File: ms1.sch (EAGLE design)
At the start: 145 parts, among them IC1 MAX3232EUE, IC2 MAX3380EEUP, J1 POWERPOLE_POWER25A, J10 Radio, J11 A3, J12 A4, J13 A5, J14 A6, J15 A7, J16 D1, J17 D2, J18 D3, J19 D4, J2 ON, J20 D5, J21 D6, J22 D7, J3 LED-EN, J4 RS232, J5 RS485, J6 A1, J7 I2C, J8 A2, J9 TTL_SERIAL, Q1 DMG6602SVT, Q2 DMG6602SVT, Q3 DMG6602SVT, Q4 DMG6602SVT, U1 LT1934ES6TRMPBF, U2 LT1934ES6TRMPBF, U3 DS3231SN, U4 ISL3179EIBZ, X1 KUSBVX-BS1N

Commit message: power supplies mostly routed
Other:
- moved on the sheet: U$2

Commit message: serial stuff laid out
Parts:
- added C26: 100nF, resistor:C-EUC0805
- renumbered VCC_3V1 to VCC_3V
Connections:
- net GND: now also C26.2
- net VCC_3V3: now also C26.1
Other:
- moved on the sheet: U$2

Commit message: added pullup to !RESET on CC1120
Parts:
- added R33: 1K, resistor:R-EU_R0805
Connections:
- new net N$17: R33.1, U$3.!RESET
- net RADIO_3V3: now also R33.2

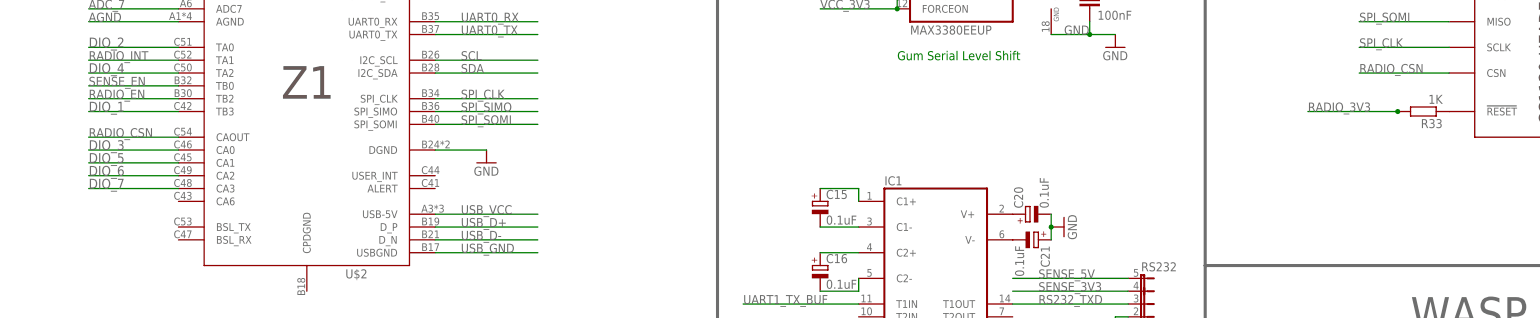
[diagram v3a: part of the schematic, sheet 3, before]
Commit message: added reset link from cc1120 to msp
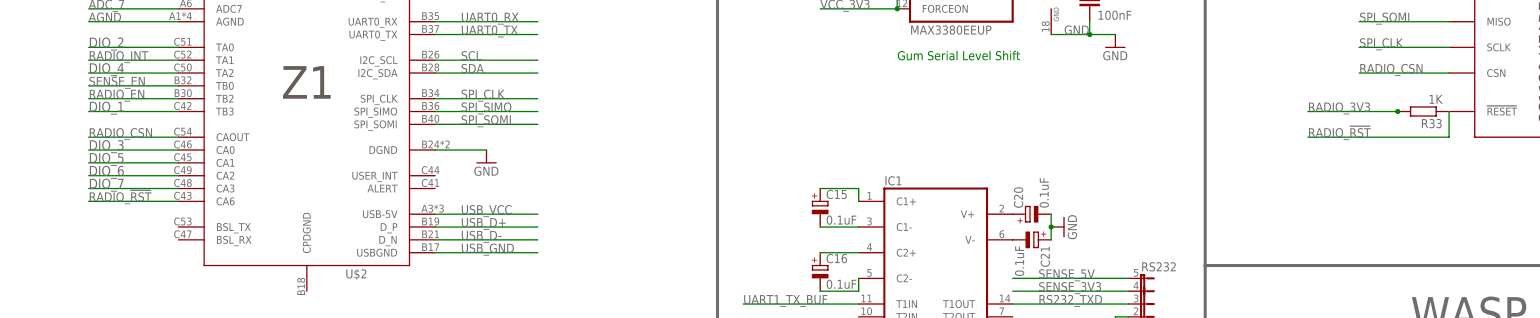
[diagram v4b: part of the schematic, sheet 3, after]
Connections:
- removed net N$17: R33.1, U$3.!RESET
- new net RADIO_!RST: R33.1, U$2.CA6, U$3.!RESET
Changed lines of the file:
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@@
 </segment>
 </net>
-<net name="N$17" class="0">
+<net name="RADIO_!RST" class="0">
+<segment>
+<pinref part="U$2" gate="G$1" pin="CA6"/>
+<wire x1="38.1" y1="167.64" x2="20.32" y2="167.64" width="0.1524" layer="91"/>
+<label x="20.32" y="167.64" size="1.778" layer="95"/>
+</segment>
 <segment>
 <pinref part="U$3" gate="G$1" pin="!RESET"/>
 <pinref part="R33" gate="G$1" pin="1"/>
+<wire x1="289.56" y1="185.42" x2="289.56" y2="180.34" width="0.1524" layer="91"/>
+<wire x1="289.56" y1="180.34" x2="261.62" y2="180.34" width="0.1524" layer="91"/>
+<label x="261.62" y="180.34" size="1.778" layer="95"/>
 </segment>
 </net>

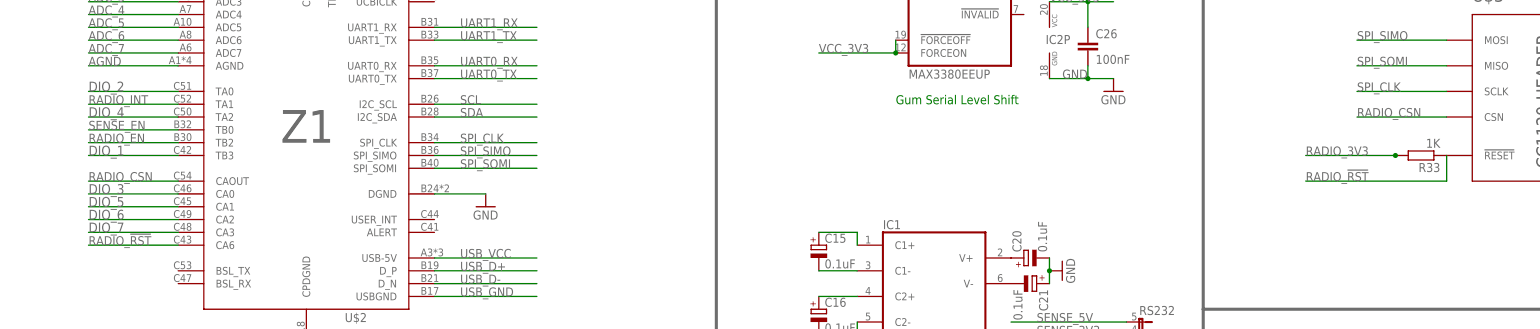
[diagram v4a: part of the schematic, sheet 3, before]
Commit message: cc1120 wiring matches test harness
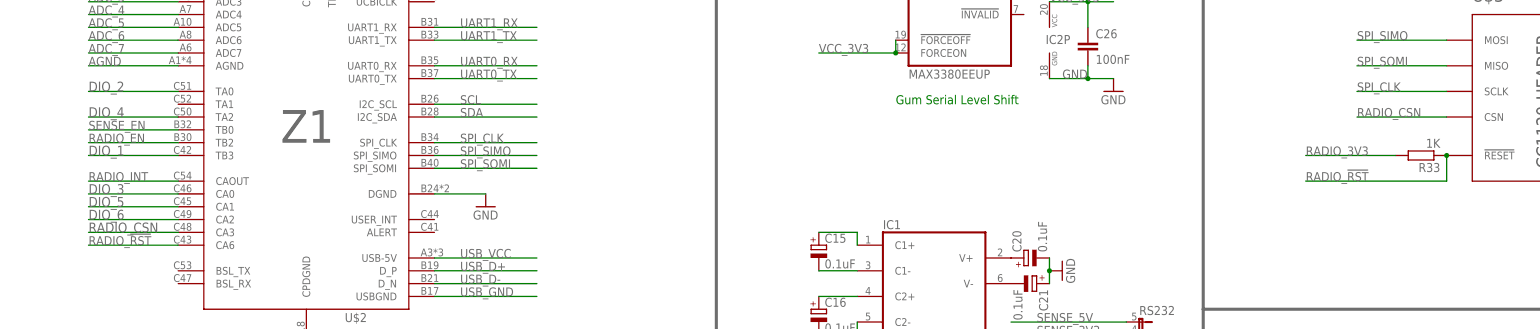
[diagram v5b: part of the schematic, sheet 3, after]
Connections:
- net DIO_7: no longer U$2.CA3
- net RADIO_CSN: now also U$2.CA3; no longer U$2.CAOUT
- net RADIO_INT: now also U$2.CAOUT; no longer U$2.TA1
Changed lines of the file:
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@@
 <label x="261.62" y="185.42" size="1.778" layer="95"/>
 <pinref part="R33" gate="G$1" pin="2"/>
-<junction x="279.4" y="185.42"/>
 </segment>
 </net>
@@
 </segment>
 <segment>
+<pinref part="U$2" gate="G$1" pin="CA3"/>
+<wire x1="38.1" y1="170.18" x2="20.32" y2="170.18" width="0.1524" layer="91"/>
+<label x="20.32" y="170.18" size="1.9304" layer="95"/>
+</segment>
+</net>
+<net name="USB_VCC" class="0">
+<segment>
+<pinref part="U$2" gate="G$1" pin="USB-5V"/>
+<wire x1="88.9" y1="165.1" x2="109.22" y2="165.1" width="0.1524" layer="91"/>
+<label x="93.98" y="165.1" size="1.778" layer="95"/>
+</segment>
+</net>
+<net name="USB_D+" class="0">
+<segment>
+<pinref part="U$2" gate="G$1" pin="D_P"/>
+<wire x1="88.9" y1="162.56" x2="109.22" y2="162.56" width="0.1524" layer="91"/>
+<label x="93.98" y="162.56" size="1.778" layer="95"/>
+</segment>
+</net>
+<net name="USB_D-" class="0">
+<segment>
+<pinref part="U$2" gate="G$1" pin="D_N"/>
+<wire x1="88.9" y1="160.02" x2="109.22" y2="160.02" width="0.1524" layer="91"/>
+<label x="93.98" y="160.02" size="1.778" layer="95"/>
+</segment>
+</net>
+<net name="USB_GND" class="0">
+<segment>
+<pinref part="U$2" gate="G$1" pin="USBGND"/>
+<wire x1="88.9" y1="157.48" x2="109.22" y2="157.48" width="0.1524" layer="91"/>
+<label x="93.98" y="157.48" size="1.778" layer="95"/>
+</segment>
+</net>
+<net name="BATV_EN" class="0">
+<segment>
+<wire x1="203.2" y1="20.32" x2="180.34" y2="20.32" width="0.1524" layer="91"/>
+<label x="182.88" y="20.32" size="1.778" layer="95"/>
+<pinref part="JP1" gate="A" pin="2"/>
+</segment>
+</net>
+<net name="SENSE_EN" class="0">
+<segment>
+<wire x1="203.2" y1="17.78" x2="180.34" y2="17.78" width="0.1524" layer="91"/>
+<label x="182.88" y="17.78" size="1.778" layer="95"/>
+<pinref part="JP1" gate="A" pin="1"/>
+</segment>
+<segment>
+<pinref part="U$2" gate="G$1" pin="TB0"/>
+<wire x1="38.1" y1="190.5" x2="20.32" y2="190.5" width="0.1524" layer="91"/>
+<label x="20.32" y="190.5" size="1.778" layer="95"/>
+</segment>
+</net>
+<net name="RADIO_EN" class="0">
+<segment>
+<wire x1="20.32" y1="187.96" x2="38.1" y2="187.96" width="0.1524" layer="91"/>
+<label x="20.32" y="187.96" size="1.778" layer="95"/>
+<pinref part="U$2" gate="G$1" pin="TB2"/>
+</segment>
+</net>
+<net name="RADIO_INT" class="0">
+<segment>
+<pinref part="U$3" gate="G$1" pin="GPIO0"/>
+<wire x1="327.66" y1="203.2" x2="350.52" y2="203.2" width="0.1524" layer="91"/>
+<label x="342.9" y="203.2" size="1.778" layer="95"/>
+</segment>
+<segment>
 <pinref part="U$2" gate="G$1" pin="CAOUT"/>
 <wire x1="38.1" y1="180.34" x2="20.32" y2="180.34" width="0.1524" layer="91"/>
 <label x="20.32" y="180.34" size="1.778" layer="95"/>
-</segment>
-</net>
-<net name="USB_VCC" class="0">
-<segment>
-<pinref part="U$2" gate="G$1" pin="USB-5V"/>
-<wire x1="88.9" y1="165.1" x2="109.22" y2="165.1" width="0.1524" layer="91"/>
-<label x="93.98" y="165.1" size="1.778" layer="95"/>
-</segment>
-</net>
-<net name="USB_D+" class="0">
-<segment>
-<pinref part="U$2" gate="G$1" pin="D_P"/>
-<wire x1="88.9" y1="162.56" x2="109.22" y2="162.56" width="0.1524" layer="91"/>
-<label x="93.98" y="162.56" size="1.778" layer="95"/>
-</segment>
-</net>
-<net name="USB_D-" class="0">
-<segment>
-<pinref part="U$2" gate="G$1" pin="D_N"/>
-<wire x1="88.9" y1="160.02" x2="109.22" y2="160.02" width="0.1524" layer="91"/>
-<label x="93.98" y="160.02" size="1.778" layer="95"/>
-</segment>
-</net>
-<net name="USB_GND" class="0">
-<segment>
-<pinref part="U$2" gate="G$1" pin="USBGND"/>
-<wire x1="88.9" y1="157.48" x2="109.22" y2="157.48" width="0.1524" layer="91"/>
-<label x="93.98" y="157.48" size="1.778" layer="95"/>
-</segment>
-</net>
-<net name="BATV_EN" class="0">
-<segment>
-<wire x1="203.2" y1="20.32" x2="180.34" y2="20.32" width="0.1524" layer="91"/>
-<label x="182.88" y="20.32" size="1.778" layer="95"/>
-<pinref part="JP1" gate="A" pin="2"/>
-</segment>
-</net>
-<net name="SENSE_EN" class="0">
-<segment>
-<wire x1="203.2" y1="17.78" x2="180.34" y2="17.78" width="0.1524" layer="91"/>
-<label x="182.88" y="17.78" size="1.778" layer="95"/>
-<pinref part="JP1" gate="A" pin="1"/>
-</segment>
-<segment>
-<pinref part="U$2" gate="G$1" pin="TB0"/>
-<wire x1="38.1" y1="190.5" x2="20.32" y2="190.5" width="0.1524" layer="91"/>
-<label x="20.32" y="190.5" size="1.778" layer="95"/>
-</segment>
-</net>
-<net name="RADIO_EN" class="0">
-<segment>
-<wire x1="20.32" y1="187.96" x2="38.1" y2="187.96" width="0.1524" layer="91"/>
-<label x="20.32" y="187.96" size="1.778" layer="95"/>
-<pinref part="U$2" gate="G$1" pin="TB2"/>
-</segment>
-</net>
-<net name="RADIO_INT" class="0">
-<segment>
-<pinref part="U$2" gate="G$1" pin="TA1"/>
-<wire x1="38.1" y1="195.58" x2="20.32" y2="195.58" width="0.1524" layer="91"/>
-<label x="20.32" y="195.58" size="1.778" layer="95"/>
-</segment>
-<segment>
-<pinref part="U$3" gate="G$1" pin="GPIO0"/>
-<wire x1="327.66" y1="203.2" x2="350.52" y2="203.2" width="0.1524" layer="91"/>
-<label x="342.9" y="203.2" size="1.778" layer="95"/>
 </segment>
 </net>
@@
 </segment>
 </net>
-<net name="DIO_7" class="0">
-<segment>
-<pinref part="U$2" gate="G$1" pin="CA3"/>
-<wire x1="38.1" y1="170.18" x2="20.32" y2="170.18" width="0.1524" layer="91"/>
-<label x="20.32" y="170.18" size="1.9304" layer="95"/>
-</segment>
-</net>
 <net name="RADIO_!RST" class="0">
 <segment>
@@
 <wire x1="289.56" y1="180.34" x2="261.62" y2="180.34" width="0.1524" layer="91"/>
 <label x="261.62" y="180.34" size="1.778" layer="95"/>
-</segment>
-</net>
+<junction x="289.56" y="185.42"/>
+</segment>
+</net>

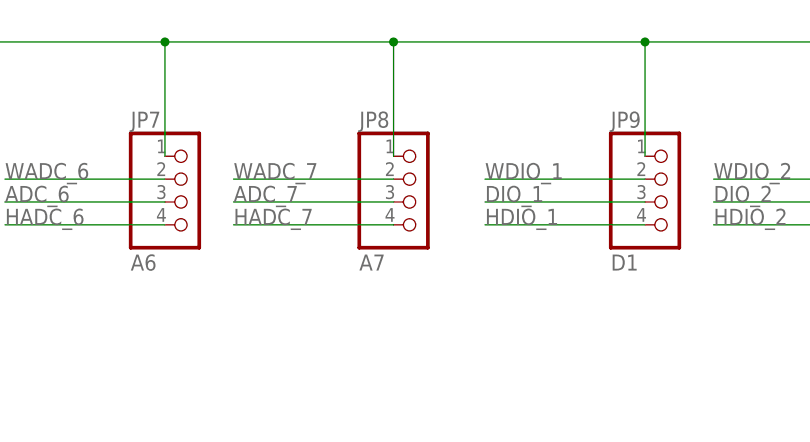
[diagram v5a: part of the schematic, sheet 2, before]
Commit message: now has cca pin
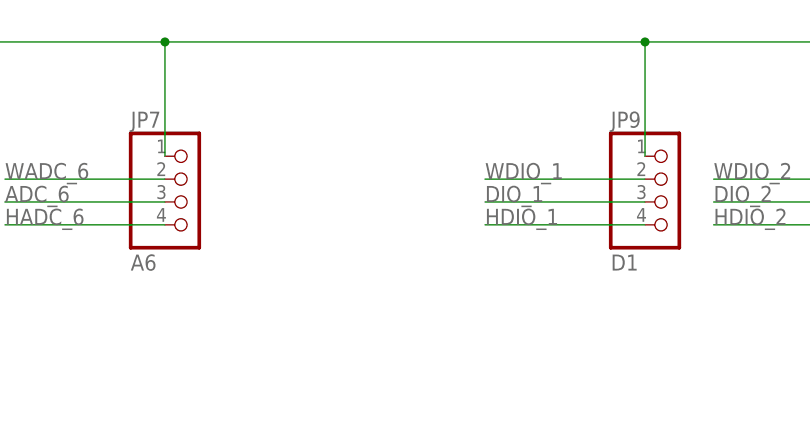
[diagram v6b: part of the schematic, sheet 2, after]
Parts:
- removed JP8: A7, pinhead:PINHD-1X4
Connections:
- removed net ADC_0: C5.1, R3.1, R4.2, U$2.ADC0
- new net RADIO_CCA_STATUS: U$2.TB3, U$3.GPIO3
- net ADC_7: now also C5.1, R3.1, R4.2; no longer JP8.3
- net DIO_1: no longer U$2.TB3
- net DIO_2: no longer U$2.TA0
- net DIO_4: no longer U$2.TA2
- net HADC_7: no longer JP8.4
- net SENSE_3V3: no longer JP8.1
- net WADC_7: no longer JP8.2
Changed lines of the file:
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@@
 <part name="JP6" library="pinhead" deviceset="PINHD-1X4" device="" value="A5"/>
 <part name="JP7" library="pinhead" deviceset="PINHD-1X4" device="" value="A6"/>
-<part name="JP8" library="pinhead" deviceset="PINHD-1X4" device="" value="A7"/>
 <part name="JP9" library="pinhead" deviceset="PINHD-1X4" device="" value="D1"/>
 <part name="JP10" library="pinhead" deviceset="PINHD-1X4" device="" value="D2"/>
@@
 </segment>
 </net>
-<net name="ADC_0" class="0">
+<net name="ADC_7" class="0">
 <segment>
 <pinref part="R4" gate="G$1" pin="2"/>
@@
 <instance part="JP6" gate="A" x="139.7" y="208.28"/>
 <instance part="JP7" gate="A" x="162.56" y="208.28"/>
-<instance part="JP8" gate="A" x="187.96" y="208.28"/>
 <instance part="JP9" gate="A" x="215.9" y="208.28"/>
 <instance part="JP10" gate="A" x="241.3" y="208.28"/>
@@
 <wire x1="114.3" y1="226.06" x2="137.16" y2="226.06" width="0.1524" layer="91"/>
 <wire x1="137.16" y1="226.06" x2="160.02" y2="226.06" width="0.1524" layer="91"/>
-<wire x1="160.02" y1="226.06" x2="185.42" y2="226.06" width="0.1524" layer="91"/>
-<wire x1="185.42" y1="226.06" x2="213.36" y2="226.06" width="0.1524" layer="91"/>
+<wire x1="160.02" y1="226.06" x2="213.36" y2="226.06" width="0.1524" layer="91"/>
 <wire x1="213.36" y1="226.06" x2="238.76" y2="226.06" width="0.1524" layer="91"/>
 <wire x1="238.76" y1="226.06" x2="264.16" y2="226.06" width="0.1524" layer="91"/>
@@
 <wire x1="35.56" y1="213.36" x2="35.56" y2="226.06" width="0.1524" layer="91"/>
 <junction x="35.56" y="226.06"/>
-<pinref part="JP8" gate="A" pin="1"/>
-<wire x1="185.42" y1="213.36" x2="185.42" y2="226.06" width="0.1524" layer="91"/>
-<junction x="185.42" y="226.06"/>
 <pinref part="JP9" gate="A" pin="1"/>
 <wire x1="213.36" y1="213.36" x2="213.36" y2="226.06" width="0.1524" layer="91"/>
@@
 </segment>
 </net>
-<net name="WADC_7" class="0">
-<segment>
-<pinref part="JP8" gate="A" pin="2"/>
-<wire x1="185.42" y1="210.82" x2="167.64" y2="210.82" width="0.1524" layer="91"/>
-<label x="167.64" y="210.82" size="1.778" layer="95"/>
-</segment>
-</net>
-<net name="ADC_7" class="0">
-<segment>
-<pinref part="JP8" gate="A" pin="3"/>
-<wire x1="185.42" y1="208.28" x2="167.64" y2="208.28" width="0.1524" layer="91"/>
-<label x="167.64" y="208.28" size="1.778" layer="95"/>
-</segment>
-</net>
 <net name="HADC_7" class="0">
-<segment>
-<pinref part="JP8" gate="A" pin="4"/>
-<wire x1="185.42" y1="205.74" x2="167.64" y2="205.74" width="0.1524" layer="91"/>
-<label x="167.64" y="205.74" size="1.778" layer="95"/>
-</segment>
 <segment>
 <pinref part="J15" gate="G$1" pin="2"/>
@@
 </segment>
 </net>
-<net name="ADC_0" class="0">
-<segment>
-<pinref part="U$2" gate="G$1" pin="ADC0"/>
-<wire x1="38.1" y1="223.52" x2="20.32" y2="223.52" width="0.1524" layer="91"/>
-<label x="20.32" y="223.52" size="1.778" layer="95"/>
-</segment>
-</net>
-<net name="DIO_2" class="0">
-<segment>
-<pinref part="U$2" gate="G$1" pin="TA0"/>
-<wire x1="38.1" y1="198.12" x2="20.32" y2="198.12" width="0.1524" layer="91"/>
-<label x="20.32" y="198.12" size="1.9304" layer="95"/>
-</segment>
-</net>
-<net name="DIO_4" class="0">
-<segment>
-<pinref part="U$2" gate="G$1" pin="TA2"/>
-<wire x1="38.1" y1="193.04" x2="20.32" y2="193.04" width="0.1524" layer="91"/>
-<label x="20.32" y="193.04" size="1.9304" layer="95"/>
-</segment>
-</net>
-<net name="DIO_1" class="0">
-<segment>
-<pinref part="U$2" gate="G$1" pin="TB3"/>
-<wire x1="38.1" y1="185.42" x2="20.32" y2="185.42" width="0.1524" layer="91"/>
-<label x="20.32" y="185.42" size="1.9304" layer="95"/>
-</segment>
-</net>
 <net name="DIO_3" class="0">
 <segment>
@@
 </segment>
 </net>
+<net name="RADIO_CCA_STATUS" class="0">
+<segment>
+<pinref part="U$3" gate="G$1" pin="GPIO3"/>
+<wire x1="327.66" y1="193.04" x2="350.52" y2="193.04" width="0.1524" layer="91"/>
+<label x="342.9" y="193.04" size="1.778" layer="95"/>
+</segment>
+<segment>
+<pinref part="U$2" gate="G$1" pin="TB3"/>
+<wire x1="38.1" y1="185.42" x2="5.08" y2="185.42" width="0.1524" layer="91"/>
+<label x="5.08" y="185.42" size="1.9304" layer="95"/>
+</segment>
+</net>

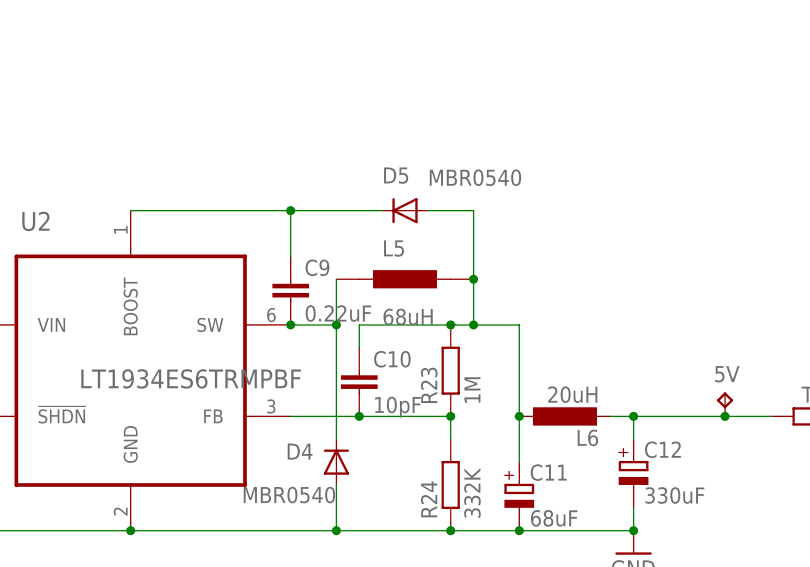
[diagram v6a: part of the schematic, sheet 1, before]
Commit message: now uses dr127 for 5w inductor
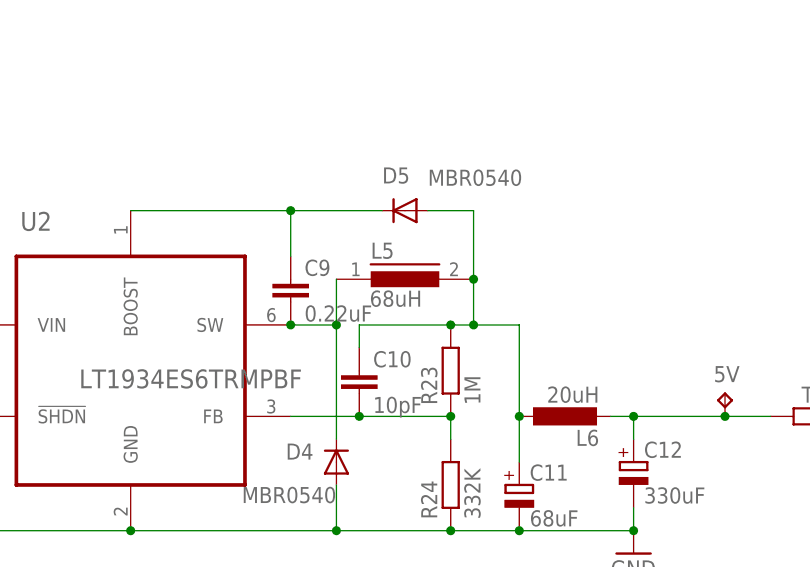
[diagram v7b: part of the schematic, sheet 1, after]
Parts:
- L5: device farnell-parts:SRU1048 -> inductors:DR127
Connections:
- net N$3: now also L5.1; no longer L5.P$1
- net N$6: now also L5.2; no longer L5.P$2
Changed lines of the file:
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@@
 <part name="R23" library="resistor" deviceset="R-EU_" device="R0805" value="1M"/>
 <part name="C10" library="resistor" deviceset="C-EU" device="C0805" value="10pF"/>
-<part name="L5" library="farnell-parts" deviceset="SRU1048" device="" value="68uH"/>
+<part name="L5" library="inductors" deviceset="DR127" device="" value="68uH"/>
 <part name="C11" library="rcl" deviceset="CPOL-EU" device="E" value="68uF"/>
 <part name="D5" library="diode" deviceset="MBR0520LT" device="" value="MBR0540"/>
@@
 <instance part="R23" gate="G$1" x="312.42" y="66.04" rot="R90"/>
 <instance part="C10" gate="G$1" x="302.26" y="66.04"/>
-<instance part="L5" gate="A" x="307.34" y="76.2"/>
+<instance part="L5" gate="G$1" x="307.34" y="76.2"/>
 <instance part="C11" gate="G$1" x="320.04" y="53.34"/>
 <instance part="D5" gate="G$1" x="307.34" y="83.82" smashed="yes" rot="R180">
@@
 <pinref part="C9" gate="G$1" pin="2"/>
 <pinref part="D4" gate="G$1" pin="C"/>
-<pinref part="L5" gate="A" pin="P$1"/>
+<pinref part="L5" gate="G$1" pin="1"/>
 </segment>
 </net>
@@
 <pinref part="C11" gate="G$1" pin="+"/>
 <pinref part="D5" gate="G$1" pin="A"/>
-<pinref part="L5" gate="A" pin="P$2"/>
+<pinref part="L5" gate="G$1" pin="2"/>
 <pinref part="R23" gate="G$1" pin="2"/>
 <pinref part="C10" gate="G$1" pin="1"/>
